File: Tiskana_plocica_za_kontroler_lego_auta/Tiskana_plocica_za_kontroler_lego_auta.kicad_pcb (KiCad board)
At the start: 2 copper layers, 16 parts, among them J1 Conn_01x02, J2 Conn_01x20, J3 Conn_01x20, J4 Conn_01x05, J5 Conn_01x02, SW1 SW_SPST

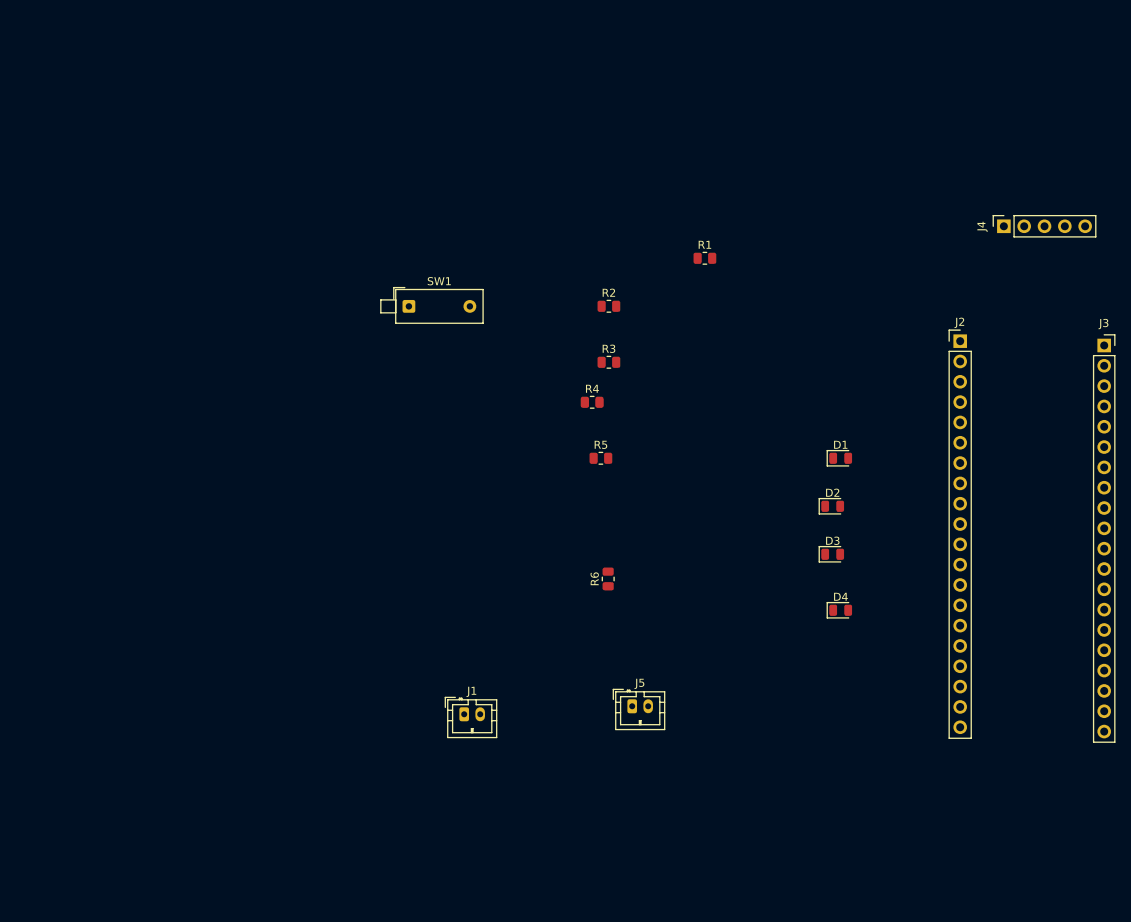
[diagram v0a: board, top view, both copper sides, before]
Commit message: PCB kontroler
poboljsanje sheme i rad na pcbu
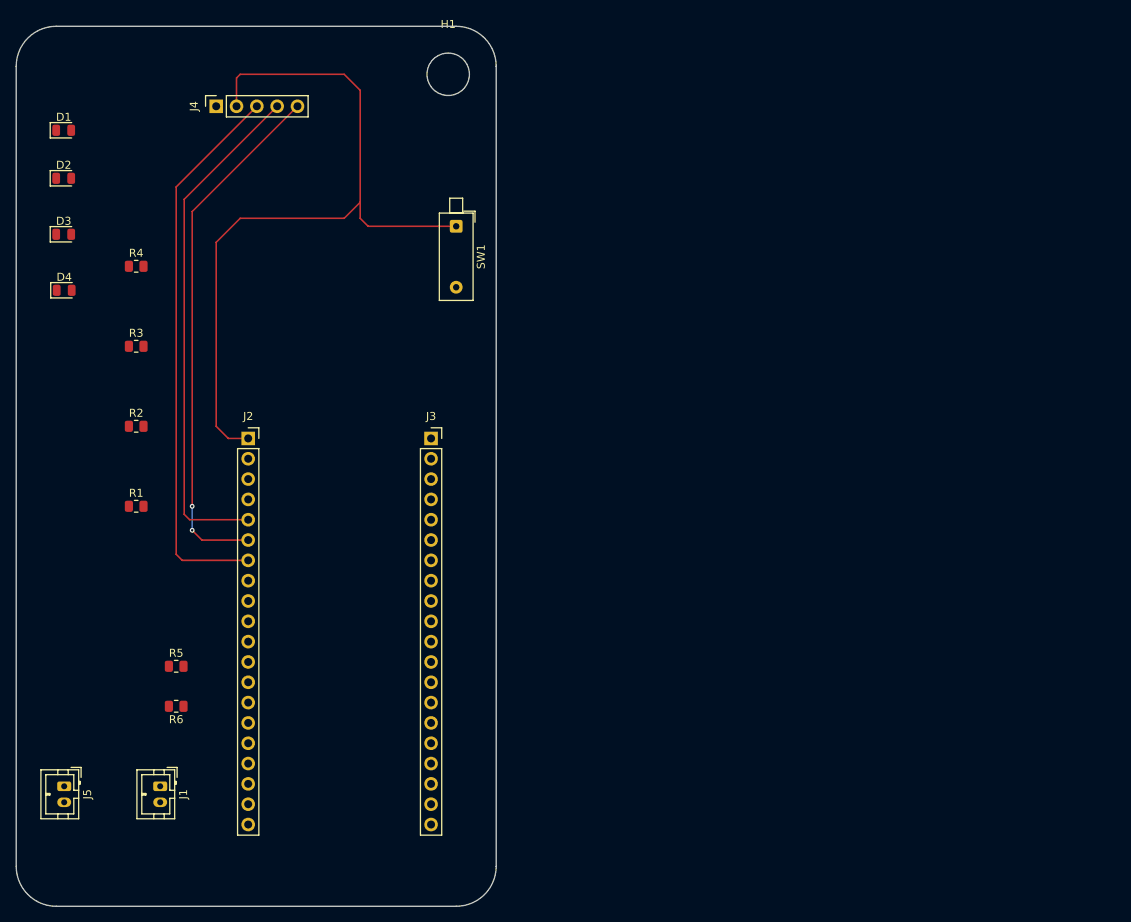
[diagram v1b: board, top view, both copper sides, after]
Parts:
- added H1: MountingHole, MountingHole:MountingHole_5.3mm_M5, F.Cu at (124.0, 46.0)
- J2: footprint Connector_PinHeader_2.54mm:PinHeader_1x20_P2.54mm_Vertical -> Connector_PinSocket_2.54mm:PinSocket_1x20_P2.54mm_Vertical
- R1, R2, R3, R4: value R -> 220
- moved D1 105.4 mm to (75.9, 53.0)
- moved D4 105.0 mm to (76.0, 73.0)
- moved D2 104.5 mm to (75.9, 59.0)
- moved D3 104.1 mm to (75.9, 66.0)
- moved J4 99.6 mm to (95.0, 50.0)
- moved J2 89.8 mm to (99.0, 91.5)
- moved J3 84.9 mm to (121.9, 91.5)
- moved R1 77.6 mm to (85.0, 100.0)
- moved J5 71.7 mm to (76.0, 135.0), turned to -90 degrees
- moved R2 61.0 mm to (85.0, 90.0)
- moved R4 59.5 mm to (85.0, 70.0)
- moved R3 59.1 mm to (85.0, 80.0)
- moved R5 59.1 mm to (90.0, 120.0)
- moved R6 56.3 mm to (90.0, 125.0), turned to 180 degrees
- moved J1 39.1 mm to (88.0, 135.0), turned to -90 degrees
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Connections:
- net Net-(D1-K) renamed gnd
- net Net-(J2-Pin_1) renamed 5V
- net Net-(J2-Pin_10) renamed BAT75
- net Net-(J2-Pin_11) renamed BAT50
- net Net-(J2-Pin_14) renamed BAT25
- net Net-(J2-Pin_8) renamed ADC
- net Net-(J2-Pin_9) renamed BAT100
- J2 pad 5: Net-(J2-Pin_5) -> ury
- J2 pad 6: Net-(J2-Pin_6) -> sw
- J2 pad 7: Net-(J2-Pin_7) -> urx
- J4 pad 3: Net-(J2-Pin_5) -> urx
- J4 pad 4: Net-(J2-Pin_6) -> ury
- J4 pad 5: Net-(J2-Pin_7) -> sw
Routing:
- net 5V: track 0.00 -> 96.1 mm
- net urx: track 0.00 -> 69.5 mm
- net sw: track 0.00 -> 66.0 mm, vias 0 -> 2
- net ury: track 0.00 -> 64.1 mm
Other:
- board outline added: 60 x 110 mm

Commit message: fix
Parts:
- moved H1 2.83 mm to (122.0, 48.0)
- moved J3 0.14 mm to (122.0, 91.5)
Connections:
- net 5V renamed +5V
- D1 pad 1: gnd -> GND
- D2 pad 1: gnd -> GND
- D3 pad 1: gnd -> GND
- D4 pad 1: gnd -> GND
- J3 pad 1: unconnected-(J3-Pin_1-Pad1) -> GND
- J3 pad 20: gnd -> unconnected-(J3-Pin_20-Pad20)
- J4 pad 1: gnd -> GND
- R6 pad 2: gnd -> GND
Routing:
- net GND: track 0.00 -> 150.3 mm, vias 0 -> 3
- net BAT25: track 0.00 -> 66.6 mm, vias 0 -> 6
- net BAT50: track 0.00 -> 47.2 mm, vias 0 -> 4
- net Net-(J2-Pin_2): track 0.00 -> 42.8 mm
- net BAT75: track 0.00 -> 34.2 mm, vias 0 -> 4
- net Net-(D4-A): track 0.00 -> 31.3 mm
- net Net-(D3-A): track 0.00 -> 28.9 mm
- net Net-(J1-Pin_1): track 0.00 -> 27.5 mm
- net Net-(D2-A): track 0.00 -> 25.3 mm
- net ADC: track 0.00 -> 22.7 mm
- net Net-(D1-A): track 0.00 -> 22.0 mm
- net BAT100: track 0.00 -> 21.0 mm, vias 0 -> 2
- net Net-(J1-Pin_2): track 0.00 -> 12.0 mm

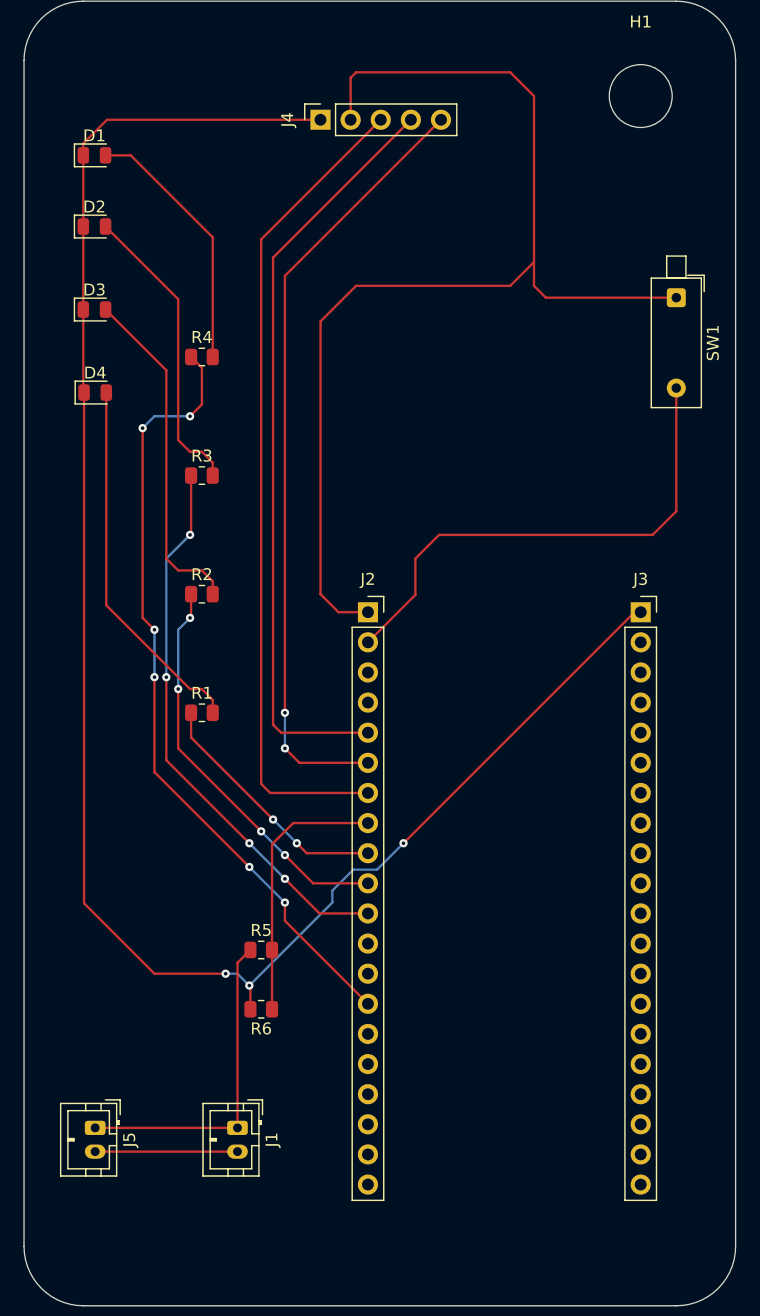
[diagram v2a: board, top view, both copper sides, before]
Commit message: Kontroler pločica final
Popravak sheme pcb-a kod kontroler pločice
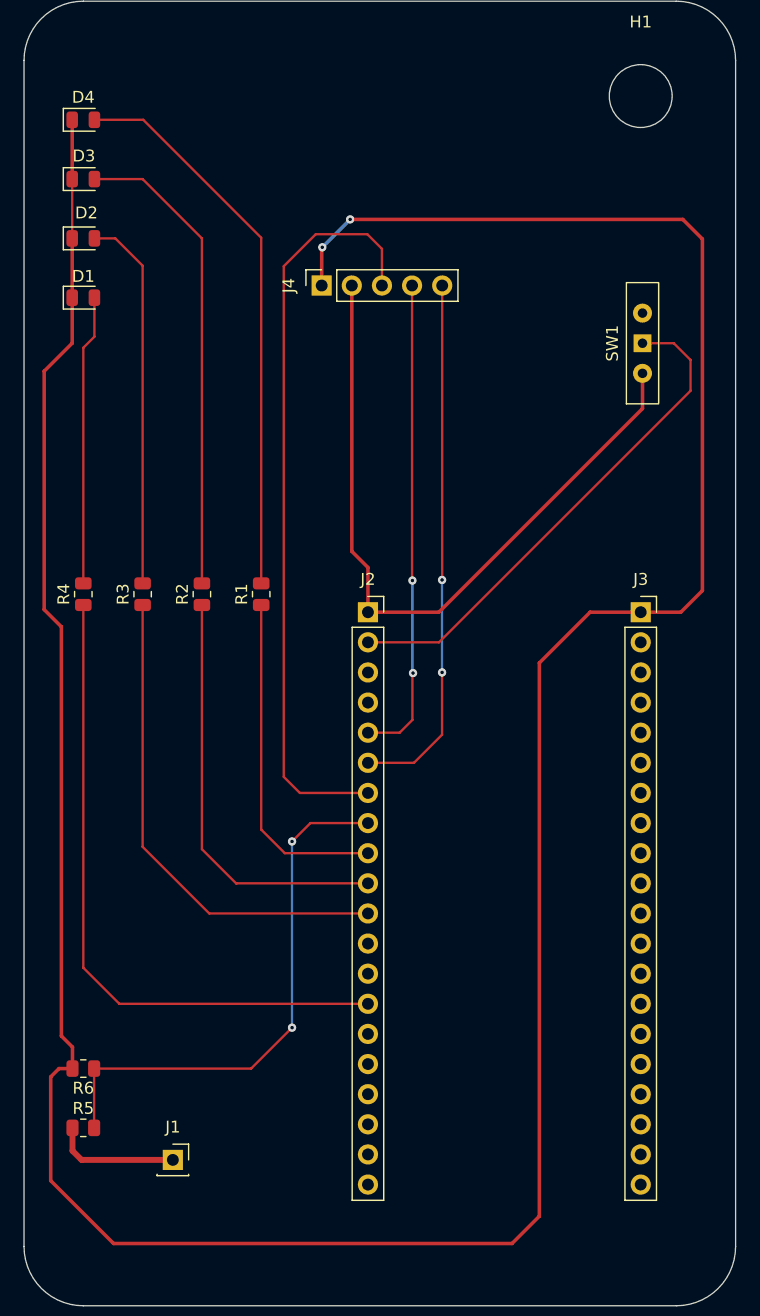
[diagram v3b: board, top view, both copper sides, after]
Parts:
- removed J5: Conn_01x02, Connector_JST:JST_PH_B2B-PH-K_1x02_P2.00mm_Vertical
- J1: value Conn_01x02 -> Conn_01x01; footprint Connector_JST:JST_PH_B2B-PH-K_1x02_P2.00mm_Vertical -> Connector_PinSocket_2.54mm:PinSocket_1x01_P2.54mm_Vertical
- SW1: value SW_SPST -> SW_SPDT; footprint Button_Switch_THT:SW_DIP_SPSTx01_Piano_10.8x4.1mm_W7.62mm_P2.54mm -> Button_Switch_THT:SW_Slide-03_Wuerth-WS-SLTV_10x2.5x6.4_P2.54mm
- moved D4 23.0 mm to (75.0, 50.0)
- moved R4 22.4 mm to (75.0, 90.0), turned to 90 degrees
- moved R5 21.2 mm to (75.0, 135.0)
- moved R6 15.8 mm to (75.0, 130.0)
- moved J4 14.0 mm to (95.1, 64.0)
- moved D1 12.0 mm to (75.0, 65.0)
- moved R1 11.2 mm to (90.0, 90.0), turned to 90 degrees
- moved R3 11.2 mm to (80.0, 90.0), turned to 90 degrees
- moved D3 11.0 mm to (75.0, 55.0)
- moved J1 6.08 mm to (82.5, 137.7), turned to 0 degrees
- moved SW1 4.78 mm to (122.2, 68.8), turned to 90 degrees
- moved D2 1.37 mm to (75.0, 60.0)
- turned R2 to 90 degrees
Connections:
- J2 pad 1: +5V -> +3.3V
- J4 pad 2: +5V -> +3.3V
- SW1 pad 1: +5V -> Net-(J2-Pin_2)
- SW1 pad 2: Net-(J2-Pin_2) -> +3.3V
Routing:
- net GND: track 150.3 -> 267.0 mm, vias 3 -> 2
- net +5V: track 96.1 -> 0.00 mm
- net +3.3V: track 0.00 -> 61.3 mm
- net ury: track 64.1 -> 40.9 mm, vias 0 -> 2
- net ADC: track 22.7 -> 45.9 mm, vias 0 -> 2
- net sw: track 66.0 -> 45.1 mm
- net Net-(J1-Pin_1): track 27.5 -> 10.7 mm
- net Net-(D4-A): track 31.3 -> 47.3 mm
- net Net-(J1-Pin_2): track 12.0 -> 0.00 mm
- net Net-(D3-A): track 28.9 -> 40.2 mm
- net BAT25: track 66.6 -> 55.8 mm, vias 6 -> 0
- net BAT100: track 21.0 -> 28.8 mm, vias 2 -> 0
- net Net-(D2-A): track 25.3 -> 31.8 mm
- net urx: track 69.5 -> 63.7 mm
- net BAT50: track 47.2 -> 41.7 mm, vias 4 -> 0
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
